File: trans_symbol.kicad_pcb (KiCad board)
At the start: 2 copper layers, 81.7 x 93.6 mm, 94 parts, among them J4 Conn_01x04, U1 ATSAMD21G18A-AU, U2 MIC5504-3.3YM5, Y1 32768Hz

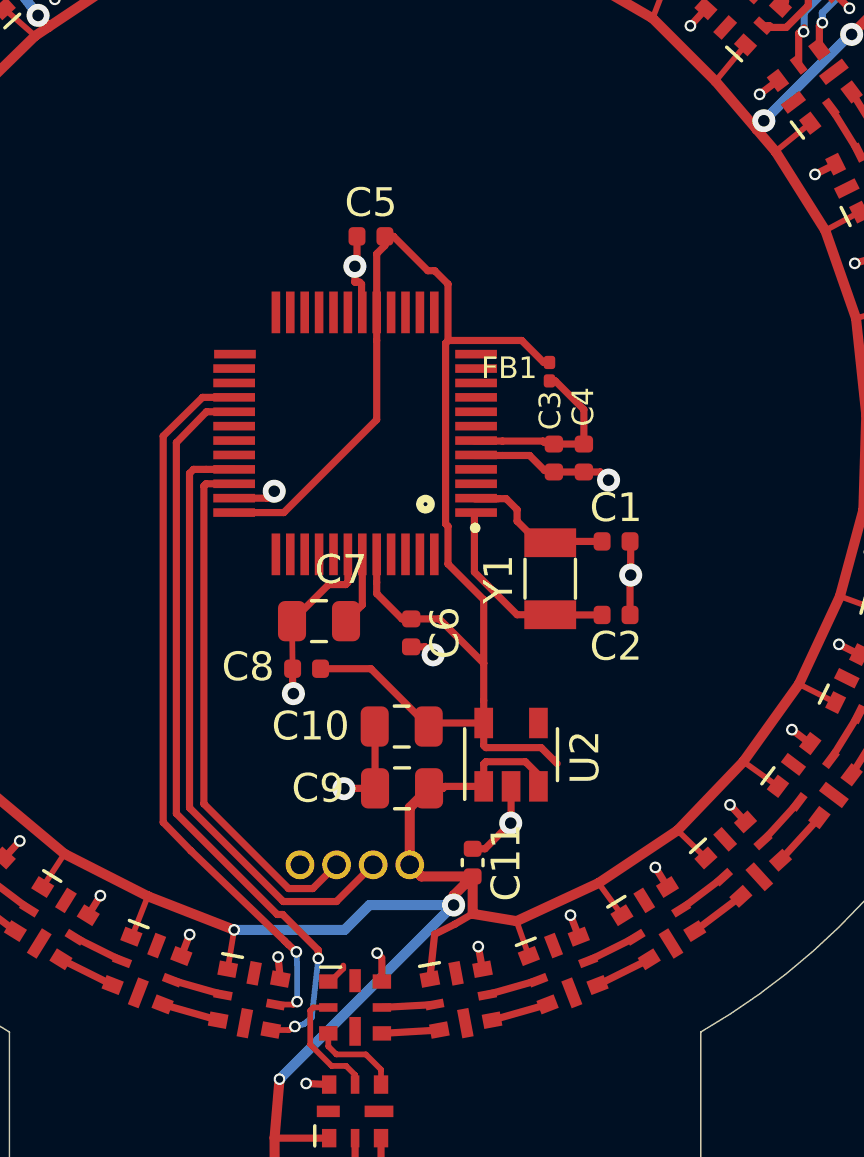
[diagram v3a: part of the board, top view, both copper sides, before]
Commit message: re-add 5V line that was removed
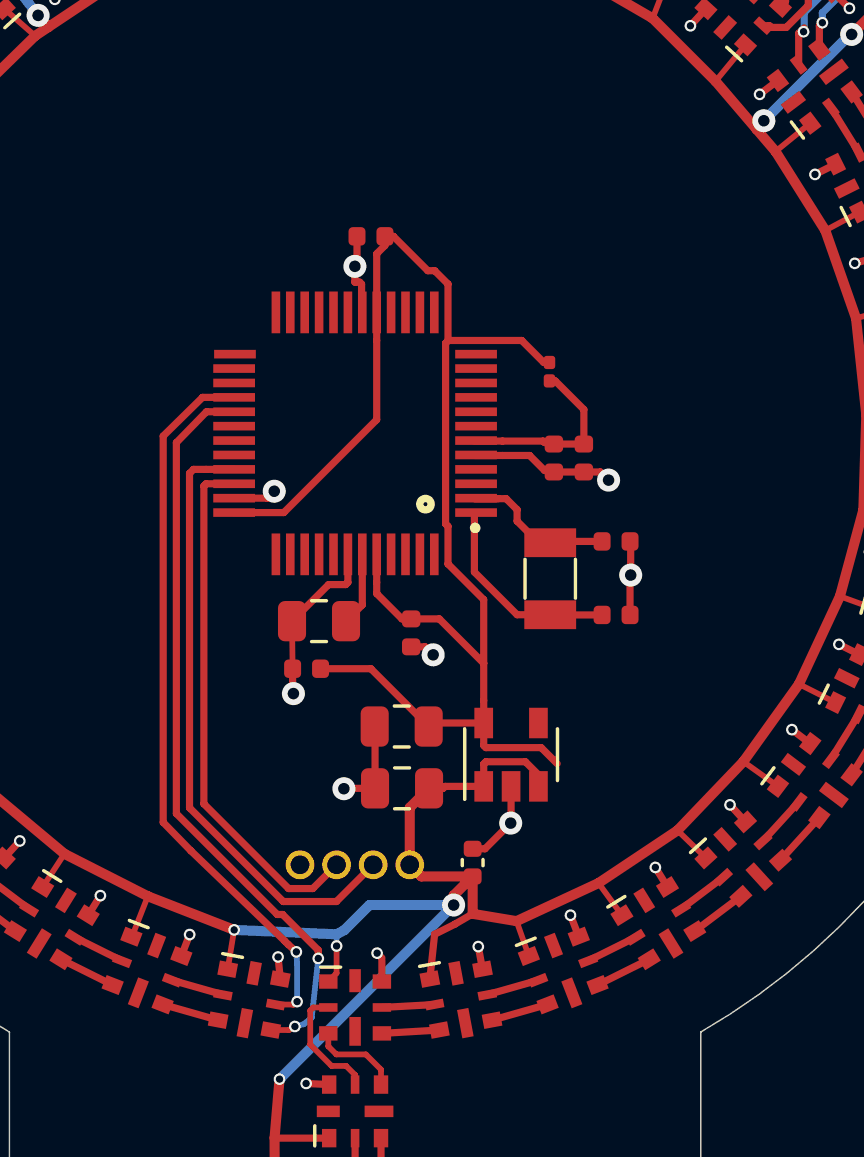
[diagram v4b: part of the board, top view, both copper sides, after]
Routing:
- net +5V: track 433.8 -> 434.8 mm, vias 15 -> 16
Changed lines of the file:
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@@
     (thickness 1.6)
     (drawings 12)
-    (tracks 936)
+    (tracks 939)
     (zones 0)
     (modules 94)
@@
   )
   (setup
-    (last_trace_width 0.35)
+    (last_trace_width 0.2)
     (user_trace_width 0.2)
     (user_trace_width 0.35)
@@
     (tags capacitor)
     (attr smd)
-    (fp_text reference C11 (at 0 -1.16 90) (layer F.SilkS)
+    (fp_text reference C11 (at 0 -1.16 90) (layer F.SilkS) hide
       (effects (font (size 1 1) (thickness 0.15)))
     )
@@
     (tags capacitor)
     (attr smd)
-    (fp_text reference C6 (at 0 -1.17 90) (layer F.SilkS)
+    (fp_text reference C6 (at 0 -1.17 90) (layer F.SilkS) hide
       (effects (font (size 1 1) (thickness 0.15)))
     )
@@
     (tags capacitor)
     (attr smd)
-    (fp_text reference C10 (at 3.1623 0.0127) (layer F.SilkS)
+    (fp_text reference C10 (at 3.1623 0.0127) (layer F.SilkS) hide
       (effects (font (size 1 1) (thickness 0.15)))
     )
@@
     (tags "SMD SMT Crystal")
     (attr smd)
-    (fp_text reference Y1 (at 0.0127 1.7907 90) (layer F.SilkS)
+    (fp_text reference Y1 (at 0.0127 1.7907 90) (layer F.SilkS) hide
       (effects (font (size 1 1) (thickness 0.15)))
     )
@@
     (fp_line (start -1.6 -0.75) (end -1.6 0.75) (layer F.Fab) (width 0.1))
     (fp_line (start -2 -1.15) (end 2 -1.15) (layer F.CrtYd) (width 0.05))
-    (fp_text user %R (at 0 -2 90) (layer F.Fab)
+    (fp_text user %R (at -0.1016 -0.0508 90) (layer F.Fab)
       (effects (font (size 1 1) (thickness 0.15)))
     )
@@
     (tags SOT-23-5)
     (attr smd)
-    (fp_text reference U2 (at -0.0889 2.5654 90) (layer F.SilkS)
+    (fp_text reference U2 (at -0.0889 2.5654 90) (layer F.SilkS) hide
       (effects (font (size 1 1) (thickness 0.15)))
     )
@@
     (tags inductor)
     (attr smd)
-    (fp_text reference FB1 (at -0.127 1.397 180) (layer F.SilkS)
+    (fp_text reference FB1 (at -0.127 1.397 180) (layer F.SilkS) hide
       (effects (font (size 0.75 0.75) (thickness 0.12)))
     )
@@
     (tags capacitor)
     (attr smd)
-    (fp_text reference C9 (at 2.921 0) (layer F.SilkS)
+    (fp_text reference C9 (at 2.921 0) (layer F.SilkS) hide
       (effects (font (size 1 1) (thickness 0.15)))
     )
@@
     (tags capacitor)
     (attr smd)
-    (fp_text reference C8 (at 2.032 0.0635) (layer F.SilkS)
+    (fp_text reference C8 (at 2.032 0.0635) (layer F.SilkS) hide
       (effects (font (size 1 1) (thickness 0.15)))
     )
@@
     (tags capacitor)
     (attr smd)
-    (fp_text reference C7 (at -0.762 1.7907) (layer F.SilkS)
+    (fp_text reference C7 (at -0.762 1.7907) (layer F.SilkS) hide
       (effects (font (size 1 1) (thickness 0.15)))
     )
@@
     (tags capacitor)
     (attr smd)
-    (fp_text reference C5 (at 0 -1.17) (layer F.SilkS)
+    (fp_text reference C5 (at 0 -1.17) (layer F.SilkS) hide
       (effects (font (size 1 1) (thickness 0.15)))
     )
@@
     (tags capacitor)
     (attr smd)
-    (fp_text reference C4 (at 1.778 -0.0254 90) (layer F.SilkS)
+    (fp_text reference C4 (at 1.778 -0.0254 90) (layer F.SilkS) hide
       (effects (font (size 0.75 0.75) (thickness 0.12)))
     )
@@
     (tags capacitor)
     (attr smd)
-    (fp_text reference C3 (at -1.651 0.127 90) (layer F.SilkS)
+    (fp_text reference C3 (at -1.651 0.127 90) (layer F.SilkS) hide
       (effects (font (size 0.75 0.75) (thickness 0.12)))
     )
@@
     (tags capacitor)
     (attr smd)
-    (fp_text reference C2 (at 0 1.0922) (layer F.SilkS)
+    (fp_text reference C2 (at 0 1.0922) (layer F.SilkS) hide
       (effects (font (size 1 1) (thickness 0.15)))
     )
@@
     (tags capacitor)
     (attr smd)
-    (fp_text reference C1 (at 0 -1.17) (layer F.SilkS)
+    (fp_text reference C1 (at 0 -1.17) (layer F.SilkS) hide
       (effects (font (size 1 1) (thickness 0.15)))
     )
@@
   (segment (start 87.7316 131.9784) (end 87.7316 133.5532) (width 0.25) (layer F.Cu) (net 7))
   (segment (start 87.7824 131.9276) (end 87.7316 131.9784) (width 0.25) (layer F.Cu) (net 7))
-  (segment (start 89.14 109.0312) (end 89.59 108.5812) (width 0.2) (layer F.Cu) (net 7))
-  (segment (start 89.07 109.0312) (end 89.14 109.0312) (width 0.2) (layer F.Cu) (net 7))
-  (segment (start 89.59 108.5812) (end 89.59 108.474632) (width 0.2) (layer F.Cu) (net 7))
   (segment (start 87.376 112.4204) (end 87.203884 114.458084) (width 0.35) (layer F.Cu) (net 7))
   (via (at 87.376 112.4204) (size 0.4064) (drill 0.254) (layers F.Cu B.Cu) (net 7))
   (segment (start 87.376 112.4204) (end 93.4212 106.3752) (width 0.35) (layer B.Cu) (net 7))
-  (segment (start 89.6366 107.2388) (end 85.8012 107.2388) (width 0.35) (layer B.Cu) (net 7))
   (segment (start 93.4212 106.3752) (end 90.5002 106.3752) (width 0.35) (layer B.Cu) (net 7))
   (segment (start 90.5002 106.3752) (end 89.6366 107.2388) (width 0.35) (layer B.Cu) (net 7))
@@
   (segment (start 92.59545 108.945672) (end 92.7608 107.3912) (width 0.25) (layer F.Cu) (net 7))
   (segment (start 87.6808 135.5344) (end 89.1 135.43) (width 0.25) (layer F.Cu) (net 7))
+  (segment (start 89.07 109.0312) (end 89.0668 109.0312) (width 0.2) (layer F.Cu) (net 7))
+  (segment (start 89.0668 109.0312) (end 89.3572 108.7408) (width 0.2) (layer F.Cu) (net 7))
+  (via (at 89.3572 107.7976) (size 0.4064) (drill 0.254) (layers F.Cu B.Cu) (net 7))
+  (segment (start 89.3572 108.7408) (end 89.3572 107.7976) (width 0.2) (layer F.Cu) (net 7))
+  (segment (start 89.3572 107.7976) (end 89.3572 107.3912) (width 0.2) (layer B.Cu) (net 7))
+  (segment (start 89.3572 107.3912) (end 85.8012 107.2388) (width 0.35) (layer B.Cu) (net 7))
+  (segment (start 89.6366 107.2388) (end 89.3572 107.3912) (width 0.35) (layer B.Cu) (net 7))
   (segment (start 85.410844 109.488574) (end 83.642365 108.985399) (width 0.25) (layer F.Cu) (net 8))
   (segment (start 85.245469 110.37325) (end 83.317248 109.824624) (width 0.25) (layer F.Cu) (net 9))

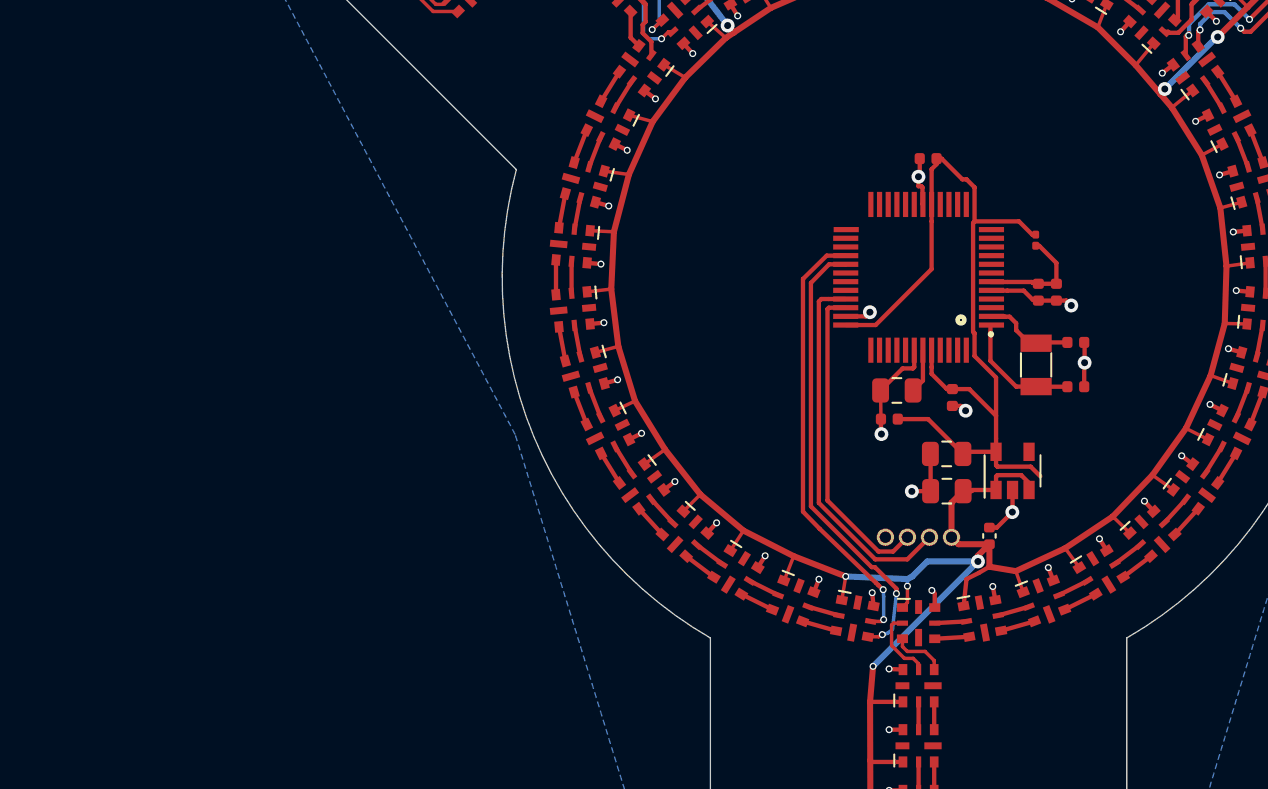
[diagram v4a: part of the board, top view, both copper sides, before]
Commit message: re-layout chip circuitry to clean it up a bit and make room for a button on each spoke; add a stub for a button
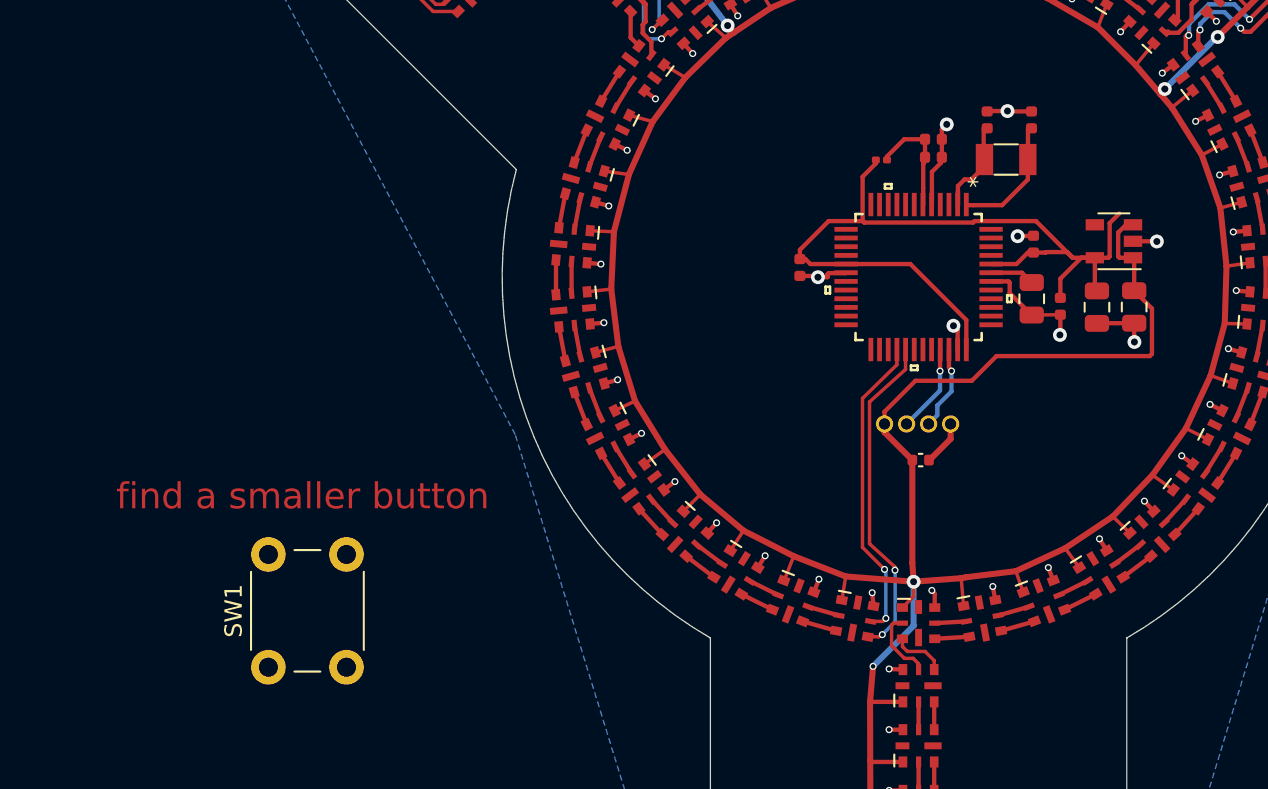
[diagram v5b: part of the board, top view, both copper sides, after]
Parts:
- added SW1: SW_SPST, Button_Switch_THT:SW_PUSH_6mm_H5mm, F.Cu at (52.5, 112.5)
- U1: footprint ATSAMD21G18A-AU:QFP50P900X900X120-48N -> ATSAMD21G18A-AU:ATSAMD21G18A-AU
- moved C2 15.6 mm to (96.5, 80.9), turned to 90 degrees
- moved C9 15.1 mm to (102.4, 91.7), turned to 270 degrees
- moved U2 14.5 mm to (101.3, 87.9), turned to 180 degrees
- moved C1 13.8 mm to (94.0, 80.9), turned to 90 degrees
- moved C10 12.1 mm to (100.3, 91.7), turned to 270 degrees
- moved Y1 12.0 mm to (95.0, 83.2), turned to 0 degrees
- moved C8 11.8 mm to (98.2, 91.7), turned to 270 degrees
- moved C4 11.3 mm to (90.9, 82.0), turned to 180 degrees
- moved FB1 10.0 mm to (87.9, 83.2), turned to 0 degrees
- moved C6 10.00 mm to (96.6, 88.1), turned to 90 degrees
- moved C3 9.85 mm to (90.9, 83.1), turned to 0 degrees
- moved C5 9.70 mm to (83.2, 89.4), turned to 90 degrees
- moved C7 9.40 mm to (96.5, 91.2), turned to 270 degrees
- moved J4 7.53 mm to (91.8, 98.5), turned to 270 degrees
- moved C11 5.90 mm to (90.1, 100.5), turned to 180 degrees
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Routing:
- net +5V: track 434.8 -> 454.4 mm, vias 16 -> 14
- net /USB_D-: track 21.5 -> 5.09 mm, vias 0 -> 1
- net /USB_D+: track 18.3 -> 4.88 mm, vias 0 -> 1
- net /APA102c LED Array/LED_SCK: track 25.6 -> 17.8 mm
- net /APA102c LED Array/LED_DATA: track 26.1 -> 19.2 mm
- net +3V3: track 51.5 -> 50.0 mm
- net GND: track 88.8 -> 90.1 mm
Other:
- board text added: "find a smaller button"

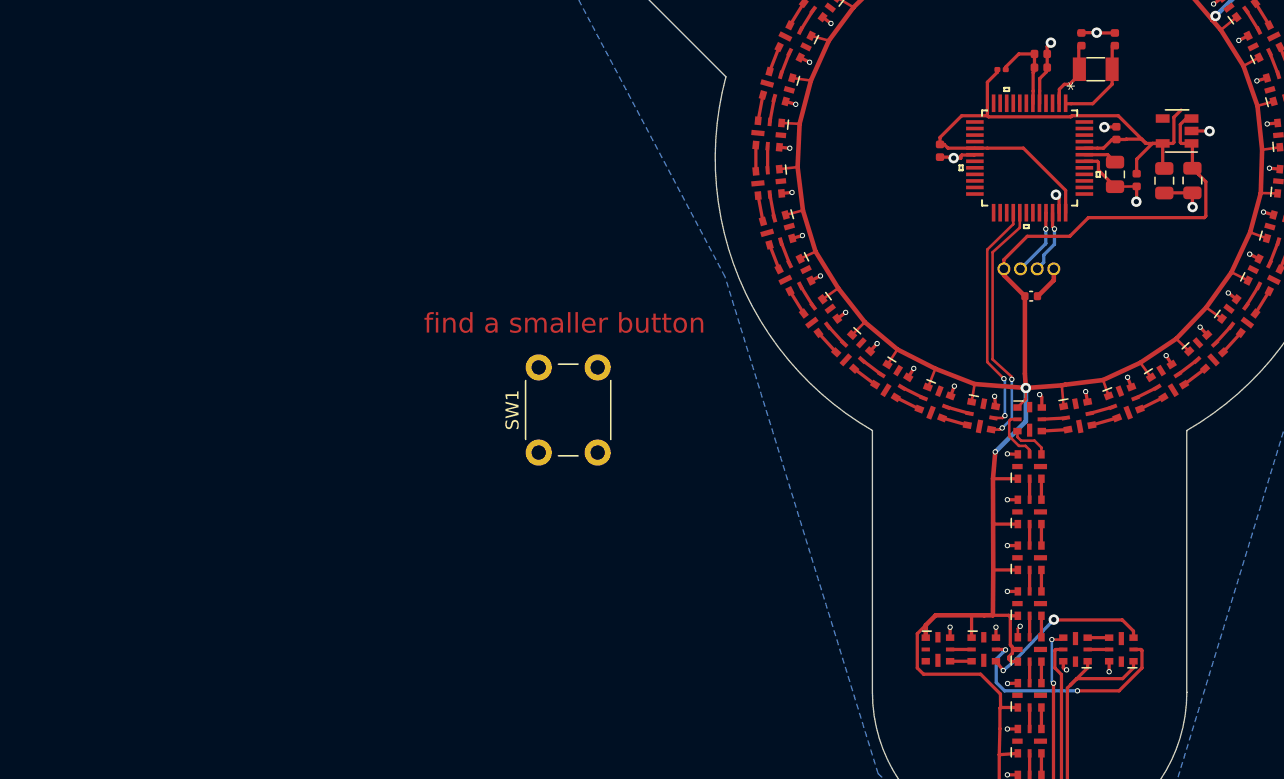
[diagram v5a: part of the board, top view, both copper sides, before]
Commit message: add an i2s microphone on default arduino zero i2s pins
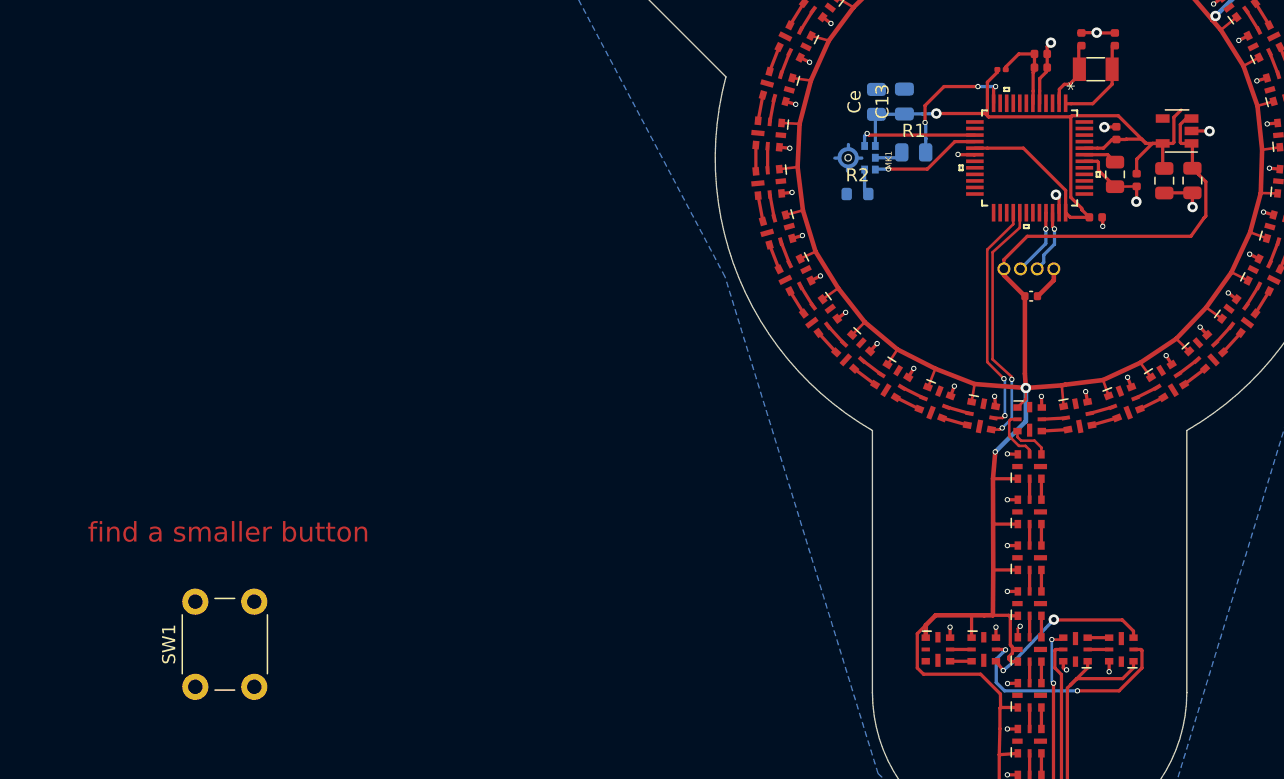
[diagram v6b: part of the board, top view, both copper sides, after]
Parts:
- added C13: 1uF, Capacitor_SMD:C_0805_2012Metric, B.Cu at (80.4, 85.7)
- added Ce: 220pF, Capacitor_SMD:C_0805_2012Metric, B.Cu at (78.3, 85.7)
- added MK1: SPH0645LM4H-B, Mic-SPH0645LM4H-B:MIC_SPH0645LM4H-B, B.Cu at (76.1, 90.0)
- added R1: 68, Resistor_SMD:R_0805_2012Metric, B.Cu at (81.2, 89.6)
- added R2: 10K, Resistor_SMD:R_0603_1608Metric, B.Cu at (76.9, 92.7)
- moved SW1 31.7 mm to (26.3, 130.4)
- moved C5 12.9 mm to (95.0, 94.5), turned to 180 degrees
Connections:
- net Net-(U1-Pad31) renamed /SDA
- net Net-(U1-Pad32) renamed /SCL
- U1 pad 12: Net-(U1-Pad12) -> /MIC_DATA
- U1 pad 15: Net-(U1-Pad15) -> /MIC_SCK_BCLK
- U1 pad 16: Net-(U1-Pad16) -> /MIC_LRCLK
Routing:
- net +3V3: track 50.0 -> 63.7 mm, vias 0 -> 1
- net /MIC_DATA: track 0.00 -> 11.0 mm, vias 0 -> 3
- net /MIC_SCK_BCLK: track 0.00 -> 9.31 mm, vias 0 -> 1
- net /MIC_LRCLK: track 0.00 -> 8.48 mm, vias 0 -> 1
- net Net-(MK1-Pad6): track 0.00 -> 2.19 mm
- net Net-(MK1-Pad2): track 0.00 -> 1.99 mm
- net (no net): track 0.00 -> 1.07 mm
- net GND: track 90.1 -> 89.6 mm, vias 85 -> 86
